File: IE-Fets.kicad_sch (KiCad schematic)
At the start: 13 parts, among them J1 PhaseOut, Q1 YJG150N03A, Q4 YJG150N03A, U4 INA185A1

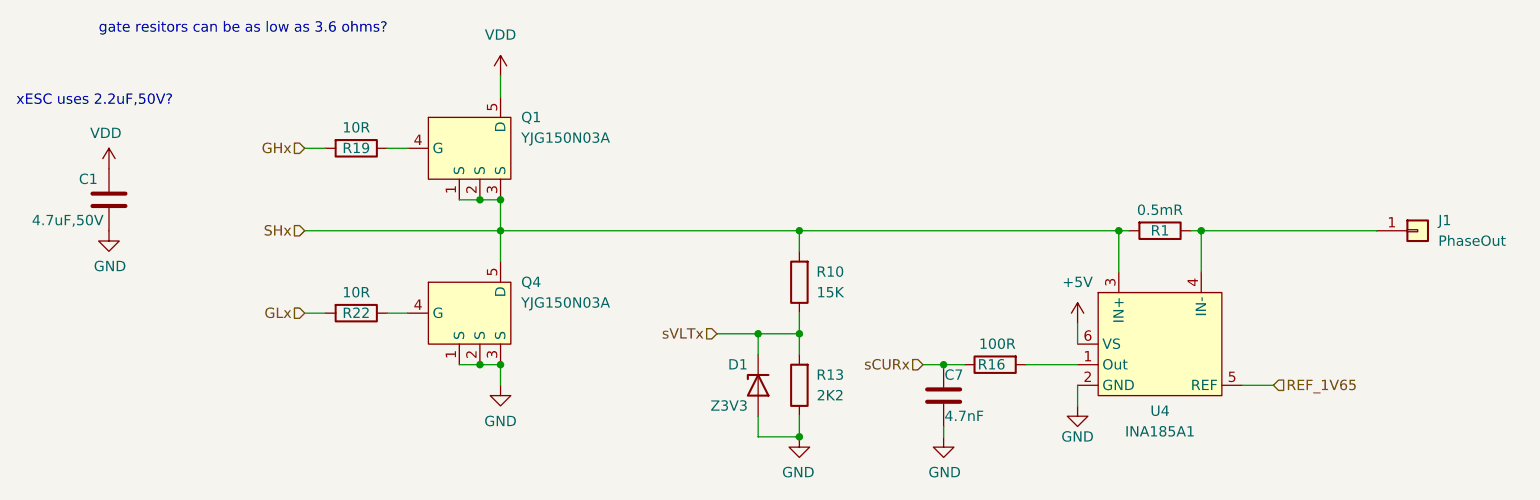
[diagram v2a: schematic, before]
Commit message: updated with g431 info
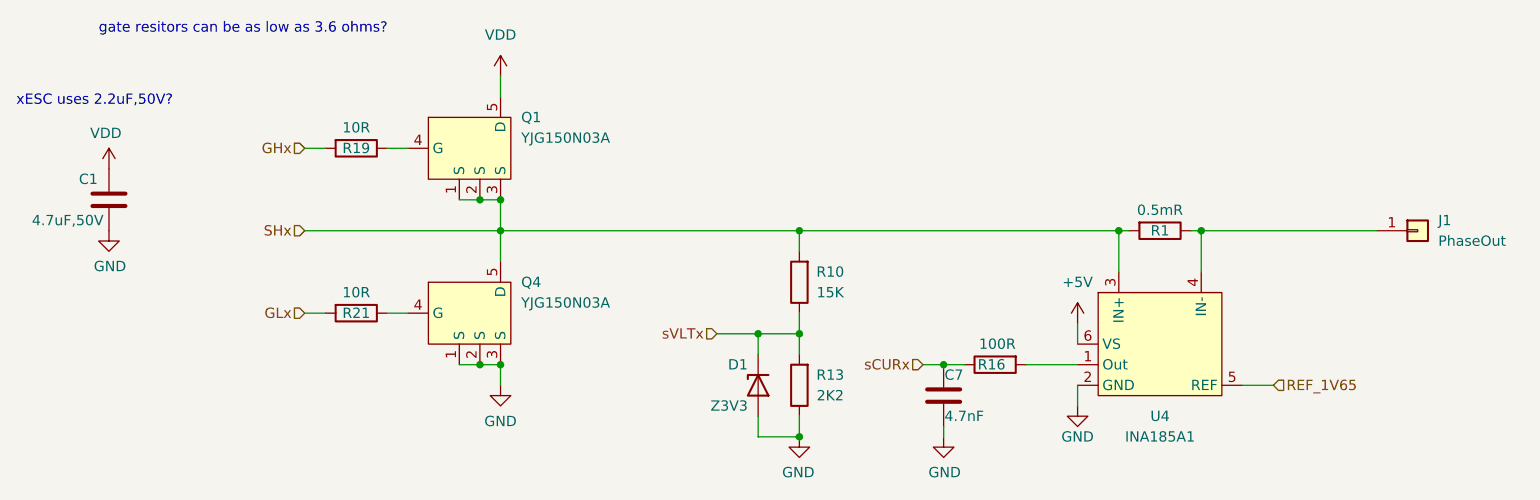
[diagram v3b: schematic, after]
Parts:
- renumbered R22 to R21
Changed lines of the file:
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@@
 				)
 				(path "/718f3b0f-9bd0-4d7b-8c07-e00d61b06ce3/946463c1-fa90-48b3-b40c-04201074b27a"
-					(reference "R19")
-					(unit 1)
-				)
-				(path "/718f3b0f-9bd0-4d7b-8c07-e00d61b06ce3/2d094a15-fef9-4d24-a2dd-8d3e0cee54dc"
-					(reference "R19")
+					(reference "R22")
+					(unit 1)
+				)
+				(path "/718f3b0f-9bd0-4d7b-8c07-e00d61b06ce3/2d094a15-fef9-4d24-a2dd-8d3e0cee54dc"
+					(reference "R24")
 					(unit 1)
 				)
@@
 				)
 				(path "/718f3b0f-9bd0-4d7b-8c07-e00d61b06ce3/946463c1-fa90-48b3-b40c-04201074b27a"
-					(reference "R16")
-					(unit 1)
-				)
-				(path "/718f3b0f-9bd0-4d7b-8c07-e00d61b06ce3/2d094a15-fef9-4d24-a2dd-8d3e0cee54dc"
-					(reference "R16")
+					(reference "R17")
+					(unit 1)
+				)
+				(path "/718f3b0f-9bd0-4d7b-8c07-e00d61b06ce3/2d094a15-fef9-4d24-a2dd-8d3e0cee54dc"
+					(reference "R18")
 					(unit 1)
 				)
@@
 				)
 				(path "/718f3b0f-9bd0-4d7b-8c07-e00d61b06ce3/946463c1-fa90-48b3-b40c-04201074b27a"
-					(reference "#PWR0163")
-					(unit 1)
-				)
-				(path "/718f3b0f-9bd0-4d7b-8c07-e00d61b06ce3/2d094a15-fef9-4d24-a2dd-8d3e0cee54dc"
-					(reference "#PWR0163")
+					(reference "#PWR0109")
+					(unit 1)
+				)
+				(path "/718f3b0f-9bd0-4d7b-8c07-e00d61b06ce3/2d094a15-fef9-4d24-a2dd-8d3e0cee54dc"
+					(reference "#PWR0120")
 					(unit 1)
 				)
@@
 				)
 				(path "/718f3b0f-9bd0-4d7b-8c07-e00d61b06ce3/946463c1-fa90-48b3-b40c-04201074b27a"
-					(reference "#PWR0165")
-					(unit 1)
-				)
-				(path "/718f3b0f-9bd0-4d7b-8c07-e00d61b06ce3/2d094a15-fef9-4d24-a2dd-8d3e0cee54dc"
-					(reference "#PWR0165")
+					(reference "#PWR0115")
+					(unit 1)
+				)
+				(path "/718f3b0f-9bd0-4d7b-8c07-e00d61b06ce3/2d094a15-fef9-4d24-a2dd-8d3e0cee54dc"
+					(reference "#PWR0180")
 					(unit 1)
 				)
@@
 				)
 				(path "/718f3b0f-9bd0-4d7b-8c07-e00d61b06ce3/946463c1-fa90-48b3-b40c-04201074b27a"
-					(reference "#PWR0102")
-					(unit 1)
-				)
-				(path "/718f3b0f-9bd0-4d7b-8c07-e00d61b06ce3/2d094a15-fef9-4d24-a2dd-8d3e0cee54dc"
-					(reference "#PWR0102")
+					(reference "#PWR0108")
+					(unit 1)
+				)
+				(path "/718f3b0f-9bd0-4d7b-8c07-e00d61b06ce3/2d094a15-fef9-4d24-a2dd-8d3e0cee54dc"
+					(reference "#PWR0178")
 					(unit 1)
 				)
@@
 				)
 				(path "/718f3b0f-9bd0-4d7b-8c07-e00d61b06ce3/946463c1-fa90-48b3-b40c-04201074b27a"
-					(reference "#PWR0101")
-					(unit 1)
-				)
-				(path "/718f3b0f-9bd0-4d7b-8c07-e00d61b06ce3/2d094a15-fef9-4d24-a2dd-8d3e0cee54dc"
-					(reference "#PWR0101")
+					(reference "#PWR0113")
+					(unit 1)
+				)
+				(path "/718f3b0f-9bd0-4d7b-8c07-e00d61b06ce3/2d094a15-fef9-4d24-a2dd-8d3e0cee54dc"
+					(reference "#PWR0179")
 					(unit 1)
 				)
@@
 				)
 				(path "/718f3b0f-9bd0-4d7b-8c07-e00d61b06ce3/946463c1-fa90-48b3-b40c-04201074b27a"
-					(reference "D1")
-					(unit 1)
-				)
-				(path "/718f3b0f-9bd0-4d7b-8c07-e00d61b06ce3/2d094a15-fef9-4d24-a2dd-8d3e0cee54dc"
-					(reference "D1")
+					(reference "D2")
+					(unit 1)
+				)
+				(path "/718f3b0f-9bd0-4d7b-8c07-e00d61b06ce3/2d094a15-fef9-4d24-a2dd-8d3e0cee54dc"
+					(reference "D3")
 					(unit 1)
 				)
@@
 				)
 				(path "/718f3b0f-9bd0-4d7b-8c07-e00d61b06ce3/946463c1-fa90-48b3-b40c-04201074b27a"
-					(reference "C7")
-					(unit 1)
-				)
-				(path "/718f3b0f-9bd0-4d7b-8c07-e00d61b06ce3/2d094a15-fef9-4d24-a2dd-8d3e0cee54dc"
-					(reference "C7")
+					(reference "C8")
+					(unit 1)
+				)
+				(path "/718f3b0f-9bd0-4d7b-8c07-e00d61b06ce3/2d094a15-fef9-4d24-a2dd-8d3e0cee54dc"
+					(reference "C9")
 					(unit 1)
 				)
@@
 				)
 				(path "/718f3b0f-9bd0-4d7b-8c07-e00d61b06ce3/946463c1-fa90-48b3-b40c-04201074b27a"
-					(reference "#PWR0112")
-					(unit 1)
-				)
-				(path "/718f3b0f-9bd0-4d7b-8c07-e00d61b06ce3/2d094a15-fef9-4d24-a2dd-8d3e0cee54dc"
-					(reference "#PWR0112")
+					(reference "#PWR0105")
+					(unit 1)
+				)
+				(path "/718f3b0f-9bd0-4d7b-8c07-e00d61b06ce3/2d094a15-fef9-4d24-a2dd-8d3e0cee54dc"
+					(reference "#PWR0117")
 					(unit 1)
 				)
@@
 				)
 				(path "/718f3b0f-9bd0-4d7b-8c07-e00d61b06ce3/946463c1-fa90-48b3-b40c-04201074b27a"
-					(reference "R10")
-					(unit 1)
-				)
-				(path "/718f3b0f-9bd0-4d7b-8c07-e00d61b06ce3/2d094a15-fef9-4d24-a2dd-8d3e0cee54dc"
-					(reference "R10")
+					(reference "R11")
+					(unit 1)
+				)
+				(path "/718f3b0f-9bd0-4d7b-8c07-e00d61b06ce3/2d094a15-fef9-4d24-a2dd-8d3e0cee54dc"
+					(reference "R12")
 					(unit 1)
 				)
@@
 				)
 				(path "/718f3b0f-9bd0-4d7b-8c07-e00d61b06ce3/946463c1-fa90-48b3-b40c-04201074b27a"
-					(reference "J1")
-					(unit 1)
-				)
-				(path "/718f3b0f-9bd0-4d7b-8c07-e00d61b06ce3/2d094a15-fef9-4d24-a2dd-8d3e0cee54dc"
-					(reference "J1")
+					(reference "J2")
+					(unit 1)
+				)
+				(path "/718f3b0f-9bd0-4d7b-8c07-e00d61b06ce3/2d094a15-fef9-4d24-a2dd-8d3e0cee54dc"
+					(reference "J3")
 					(unit 1)
 				)
@@
 		(on_board yes)
 		(dnp no)
-		(property "Reference" "R22"
+		(property "Reference" "R21"
 			(at 115.57 69.85 90)
 			(effects
@@
 			(project "I3ESC"
 				(path "/718f3b0f-9bd0-4d7b-8c07-e00d61b06ce3/dd0aac2e-62bc-46c0-bbcd-34b6d0f35d42"
-					(reference "R22")
-					(unit 1)
-				)
-				(path "/718f3b0f-9bd0-4d7b-8c07-e00d61b06ce3/946463c1-fa90-48b3-b40c-04201074b27a"
-					(reference "R22")
-					(unit 1)
-				)
-				(path "/718f3b0f-9bd0-4d7b-8c07-e00d61b06ce3/2d094a15-fef9-4d24-a2dd-8d3e0cee54dc"
-					(reference "R22")
+					(reference "R21")
+					(unit 1)
+				)
+				(path "/718f3b0f-9bd0-4d7b-8c07-e00d61b06ce3/946463c1-fa90-48b3-b40c-04201074b27a"
+					(reference "R23")
+					(unit 1)
+				)
+				(path "/718f3b0f-9bd0-4d7b-8c07-e00d61b06ce3/2d094a15-fef9-4d24-a2dd-8d3e0cee54dc"
+					(reference "R25")
 					(unit 1)
 				)
@@
 				)
 				(path "/718f3b0f-9bd0-4d7b-8c07-e00d61b06ce3/946463c1-fa90-48b3-b40c-04201074b27a"
-					(reference "R1")
-					(unit 1)
-				)
-				(path "/718f3b0f-9bd0-4d7b-8c07-e00d61b06ce3/2d094a15-fef9-4d24-a2dd-8d3e0cee54dc"
-					(reference "R1")
+					(reference "R2")
+					(unit 1)
+				)
+				(path "/718f3b0f-9bd0-4d7b-8c07-e00d61b06ce3/2d094a15-fef9-4d24-a2dd-8d3e0cee54dc"
+					(reference "R3")
 					(unit 1)
 				)
@@
 				)
 				(path "/718f3b0f-9bd0-4d7b-8c07-e00d61b06ce3/946463c1-fa90-48b3-b40c-04201074b27a"
-					(reference "C1")
-					(unit 1)
-				)
-				(path "/718f3b0f-9bd0-4d7b-8c07-e00d61b06ce3/2d094a15-fef9-4d24-a2dd-8d3e0cee54dc"
-					(reference "C1")
+					(reference "C2")
+					(unit 1)
+				)
+				(path "/718f3b0f-9bd0-4d7b-8c07-e00d61b06ce3/2d094a15-fef9-4d24-a2dd-8d3e0cee54dc"
+					(reference "C3")
 					(unit 1)
 				)
@@
 				)
 				(path "/718f3b0f-9bd0-4d7b-8c07-e00d61b06ce3/946463c1-fa90-48b3-b40c-04201074b27a"
-					(reference "R13")
-					(unit 1)
-				)
-				(path "/718f3b0f-9bd0-4d7b-8c07-e00d61b06ce3/2d094a15-fef9-4d24-a2dd-8d3e0cee54dc"
-					(reference "R13")
+					(reference "R14")
+					(unit 1)
+				)
+				(path "/718f3b0f-9bd0-4d7b-8c07-e00d61b06ce3/2d094a15-fef9-4d24-a2dd-8d3e0cee54dc"
+					(reference "R15")
 					(unit 1)
 				)
@@
 		(fields_autoplaced yes)
 		(property "Reference" "U4"
-			(at 214.63 81.915 0)
+			(at 214.63 82.55 0)
 			(effects
 				(font
@@
 		)
 		(property "Value" "INA185A1"
-			(at 214.63 84.455 0)
+			(at 214.63 85.09 0)
 			(effects
 				(font
@@
 				)
 				(path "/718f3b0f-9bd0-4d7b-8c07-e00d61b06ce3/946463c1-fa90-48b3-b40c-04201074b27a"
-					(reference "U4")
-					(unit 1)
-				)
-				(path "/718f3b0f-9bd0-4d7b-8c07-e00d61b06ce3/2d094a15-fef9-4d24-a2dd-8d3e0cee54dc"
-					(reference "U4")
+					(reference "U5")
+					(unit 1)
+				)
+				(path "/718f3b0f-9bd0-4d7b-8c07-e00d61b06ce3/2d094a15-fef9-4d24-a2dd-8d3e0cee54dc"
+					(reference "U6")
 					(unit 1)
 				)
@@
 				)
 				(path "/718f3b0f-9bd0-4d7b-8c07-e00d61b06ce3/946463c1-fa90-48b3-b40c-04201074b27a"
-					(reference "#PWR0164")
-					(unit 1)
-				)
-				(path "/718f3b0f-9bd0-4d7b-8c07-e00d61b06ce3/2d094a15-fef9-4d24-a2dd-8d3e0cee54dc"
-					(reference "#PWR0164")
+					(reference "#PWR0110")
+					(unit 1)
+				)
+				(path "/718f3b0f-9bd0-4d7b-8c07-e00d61b06ce3/2d094a15-fef9-4d24-a2dd-8d3e0cee54dc"
+					(reference "#PWR0121")
 					(unit 1)
 				)
@@
 				)
 				(path "/718f3b0f-9bd0-4d7b-8c07-e00d61b06ce3/946463c1-fa90-48b3-b40c-04201074b27a"
-					(reference "Q1")
-					(unit 1)
-				)
-				(path "/718f3b0f-9bd0-4d7b-8c07-e00d61b06ce3/2d094a15-fef9-4d24-a2dd-8d3e0cee54dc"
-					(reference "Q1")
+					(reference "Q2")
+					(unit 1)
+				)
+				(path "/718f3b0f-9bd0-4d7b-8c07-e00d61b06ce3/2d094a15-fef9-4d24-a2dd-8d3e0cee54dc"
+					(reference "Q3")
 					(unit 1)
 				)
@@
 				)
 				(path "/718f3b0f-9bd0-4d7b-8c07-e00d61b06ce3/946463c1-fa90-48b3-b40c-04201074b27a"
-					(reference "Q4")
-					(unit 1)
-				)
-				(path "/718f3b0f-9bd0-4d7b-8c07-e00d61b06ce3/2d094a15-fef9-4d24-a2dd-8d3e0cee54dc"
-					(reference "Q4")
+					(reference "Q5")
+					(unit 1)
+				)
+				(path "/718f3b0f-9bd0-4d7b-8c07-e00d61b06ce3/2d094a15-fef9-4d24-a2dd-8d3e0cee54dc"
+					(reference "Q6")
 					(unit 1)
 				)
@@
 				)
 				(path "/718f3b0f-9bd0-4d7b-8c07-e00d61b06ce3/946463c1-fa90-48b3-b40c-04201074b27a"
-					(reference "#PWR0166")
-					(unit 1)
-				)
-				(path "/718f3b0f-9bd0-4d7b-8c07-e00d61b06ce3/2d094a15-fef9-4d24-a2dd-8d3e0cee54dc"
-					(reference "#PWR0166")
+					(reference "#PWR0116")
+					(unit 1)
+				)
+				(path "/718f3b0f-9bd0-4d7b-8c07-e00d61b06ce3/2d094a15-fef9-4d24-a2dd-8d3e0cee54dc"
+					(reference "#PWR0181")
 					(unit 1)
 				)
@@
 				)
 				(path "/718f3b0f-9bd0-4d7b-8c07-e00d61b06ce3/946463c1-fa90-48b3-b40c-04201074b27a"
-					(reference "#PWR0103")
-					(unit 1)
-				)
-				(path "/718f3b0f-9bd0-4d7b-8c07-e00d61b06ce3/2d094a15-fef9-4d24-a2dd-8d3e0cee54dc"
-					(reference "#PWR0103")
-					(unit 1)
-				)
+					(reference "#PWR0111")
+					(unit 1)
+				)
+				(path "/718f3b0f-9bd0-4d7b-8c07-e00d61b06ce3/2d094a15-fef9-4d24-a2dd-8d3e0cee54dc"
+					(reference "#PWR0122")
+					(unit 1)
+				)
